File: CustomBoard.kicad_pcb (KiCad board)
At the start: 4 copper layers, 40.9 x 34.1 mm, 24 parts, among them J1 RIGHT, J10 Sensor08, J11 Sensor09, J12 Sensor10, J13 Sensor11, J14 Sensor12, J2 LEFT, J3 Sensor01, J4 Sensor02, J5 Sensor03, J6 Sensor04, J7 Sensor05, J8 Sensor06, J9 Sensor07, U1 DS28E05, U2 PCA9555, U3 VL53L1X

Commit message: routing power lines
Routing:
- net VCC: track 0.00 -> 146.8 mm, vias 0 -> 12
- net GND: track 0.00 -> 138.5 mm, vias 0 -> 12
- net SDA: track 122.2 -> 134.0 mm
- net OW: track 0.00 -> 6.91 mm
- added copper zone on F.Cu, net GND

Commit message: continue routing
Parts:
- added R10: 10k, Resistors_SMD:R_0402, B.Cu at (135.4, 111.7)
- added R11: 10k, Resistors_SMD:R_0402, B.Cu at (127.2, 111.4)
- added R12: 10k, Resistors_SMD:R_0402, B.Cu at (122.6, 103.4)
- added R13: 10k, Resistors_SMD:R_0402, B.Cu at (123.2, 94.2)
- added R14: 10k, Resistors_SMD:R_0402, B.Cu at (125.5, 86.0)
- added R2: 10k, Resistors_SMD:R_0402, B.Cu at (132.9, 82.3)
- added R3: 10k, Resistors_SMD:R_0402, B.Cu at (141.7, 82.3)
- added R5: 10k, Resistors_SMD:R_0402, B.Cu at (150.8, 82.3)
- added R6: 10k, Resistors_SMD:R_0402, B.Cu at (155.6, 90.1)
- added R7: 10k, Resistors_SMD:R_0402, B.Cu at (155.1, 100.4)
- added R8: 10k, Resistors_SMD:R_0402, B.Cu at (152.0, 107.6)
- added R9: 10k, Resistors_SMD:R_0402, B.Cu at (145.5, 111.6)
- J2: footprint Pin_Header_Straight_1x10_Pitch2.00mm_SMD_Pin1Left -> Pin_Headers:Pin_Header_Straight_1x10_Pitch2.00mm_SMD_Pin1Left
- moved J8 38.6 mm to (155.3, 107.3), turned to 45 degrees
- moved J14 38.5 mm to (122.7, 86.7), turned to 225 degrees
- moved J13 31.9 mm to (120.9, 97.0), turned to 270 degrees
- moved J7 31.9 mm to (157.1, 97.0), turned to 90 degrees
- moved J3 31.9 mm to (129.7, 80.6), turned to 180 degrees
- moved J9 31.8 mm to (148.3, 113.3), turned to 0 degrees
- moved J4 17.4 mm to (139.0, 80.6), turned to 180 degrees
- moved J6 17.4 mm to (155.3, 86.7), turned to 135 degrees
- moved J12 17.4 mm to (122.7, 107.3), turned to 315 degrees
- moved J10 17.4 mm to (139.0, 113.3), turned to 0 degrees
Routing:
- net GND: track 138.5 -> 210.2 mm, vias 12 -> 15
- net S03: track 0.00 -> 30.0 mm
- net S04: track 0.00 -> 29.0 mm
- net S05: track 0.00 -> 27.5 mm
- net S06: track 0.00 -> 26.5 mm
- net S07: track 0.00 -> 25.8 mm
- net S02: track 0.00 -> 20.4 mm
- net S01: track 0.00 -> 19.3 mm
- net S08: track 0.00 -> 18.2 mm
- net S09: track 0.00 -> 18.0 mm
- net S12: track 0.00 -> 17.9 mm
- net S10: track 0.00 -> 14.2 mm
- net S11: track 0.00 -> 11.5 mm
- net S15: track 0.00 -> 9.47 mm, vias 0 -> 1
- net VCC: track 146.8 -> 154.1 mm

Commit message: continue routing ..
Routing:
- net VCC: track 154.1 -> 193.6 mm, vias 12 -> 14
- net SCL: track 132.8 -> 160.3 mm, vias 12 -> 14
- net SDA: track 134.0 -> 158.9 mm, vias 12 -> 14
- net Net-(D1-Pad1): track 0.00 -> 23.0 mm, vias 0 -> 2
- net Net-(D1-Pad2): track 0.00 -> 3.44 mm, vias 0 -> 1
- net GND: track 210.2 -> 212.1 mm
- added copper zone on B.Cu, net VCC

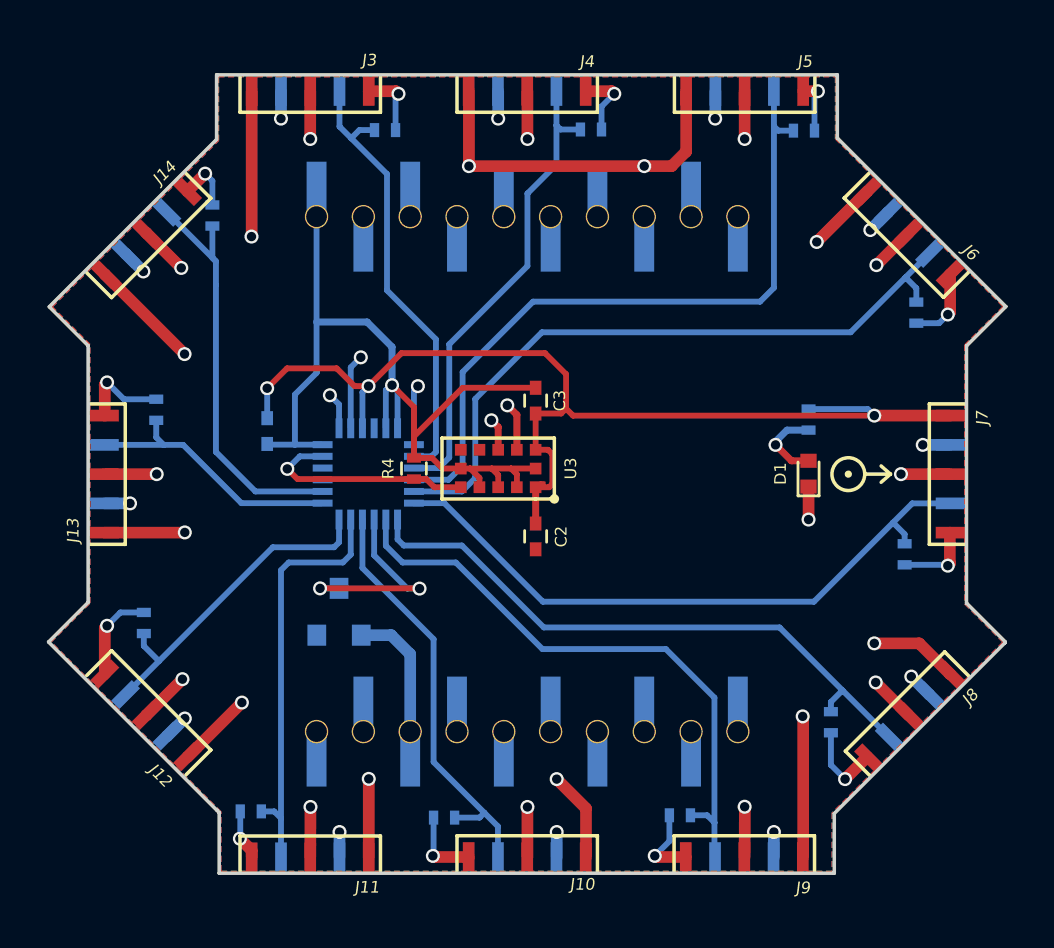
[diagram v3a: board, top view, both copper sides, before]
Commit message: pads missing
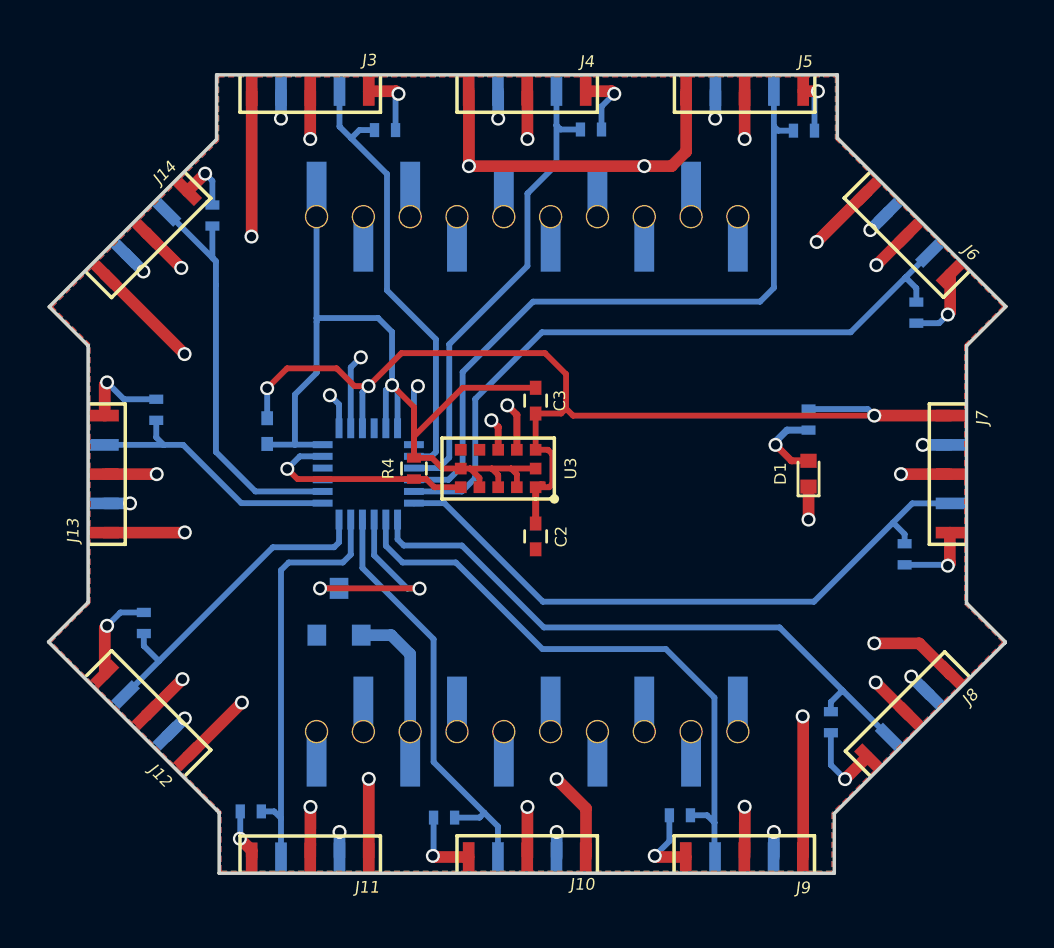
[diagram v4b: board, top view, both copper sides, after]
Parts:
- removed EXP_ORIENTATION: VAL**, crazy2libs:EXP_ORIENTATION
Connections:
- J2 pad 2: (no net) -> Net-(J2-Pad2)
- J2 pad 3: (no net) -> Net-(J2-Pad3)
- J2 pad 6: (no net) -> Net-(J2-Pad6)
- J2 pad 7: (no net) -> Net-(J2-Pad7)
- J2 pad 8: (no net) -> Net-(J2-Pad8)
- J2 pad 9: (no net) -> Net-(J2-Pad9)
- U2 pad 15: S13 -> (no net)
- U2 pad 16: S14 -> (no net)
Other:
- rule trace_min: 0.1 -> 0.05

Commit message: footprints back
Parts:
- J1: footprint Pin_Header_Straight_1x10_Pitch2.00mm_SMD_Pin1Right -> Pin_Headers:Pin_Header_Straight_1x10_Pitch2.00mm_SMD_Pin1Right
- moved C3 0.93 mm to (140.1, 93.3), turned to 180 degrees
- moved C2 0.78 mm to (139.9, 99.1), turned to 0 degrees
- moved J12 0.16 mm to (122.6, 107.4)
- moved J14 0.11 mm to (122.7, 86.6)
- moved J9 0.10 mm to (148.3, 113.5)
- moved J10 0.10 mm to (139.0, 113.5)
- moved J3 0.10 mm to (129.7, 80.5)
- moved J6 0.09 mm to (155.4, 86.6)
- moved J5 0.09 mm to (148.3, 80.5)
- moved J4 0.07 mm to (139.0, 80.6)
- moved J13 0.07 mm to (120.9, 97.0)
- moved J8 0.06 mm to (155.4, 107.4)
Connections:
- J1 pad 1: (no net) -> Net-(J1-Pad1)
- J1 pad 10: (no net) -> Net-(J1-Pad10)
- J1 pad 2: (no net) -> Net-(J1-Pad2)
- J1 pad 3: (no net) -> Net-(J1-Pad3)
- J1 pad 4: (no net) -> Net-(J1-Pad4)
- J1 pad 5: (no net) -> Net-(J1-Pad5)
- J1 pad 6: (no net) -> Net-(J1-Pad6)
- J1 pad 7: (no net) -> Net-(J1-Pad7)
- J1 pad 9: (no net) -> Net-(J1-Pad9)

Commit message: footprints back all
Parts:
- moved C2 0.55 mm to (139.9, 99.7)
- moved C3 0.38 mm to (140.1, 93.7)
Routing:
- net VCC: track 194.0 -> 194.5 mm

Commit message: complete board
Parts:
- J1: footprint Pin_Headers:Pin_Header_Straight_1x10_Pitch2.00mm_SMD_Pin1Right -> footprint:BF090-10-X-B2
- J2: footprint Pin_Headers:Pin_Header_Straight_1x10_Pitch2.00mm_SMD_Pin1Left -> footprint:BF090-10-X-B2
- turned J1 to 180 degrees
- turned J2 to 180 degrees
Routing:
- net SCL: track 160.3 -> 161.9 mm
- net GND: track 212.9 -> 214.5 mm
- net Net-(J2-Pad9): track 0.00 -> 1.60 mm
- net Net-(J2-Pad8): track 0.00 -> 1.60 mm
- net Net-(J2-Pad7): track 0.00 -> 1.60 mm
- net Net-(J2-Pad6): track 0.00 -> 1.60 mm
- net Net-(J2-Pad3): track 0.00 -> 1.60 mm
- net Net-(J2-Pad2): track 0.00 -> 1.60 mm
- net Net-(J1-Pad9): track 0.00 -> 1.60 mm
- net Net-(J1-Pad7): track 0.00 -> 1.60 mm
- net Net-(J1-Pad6): track 0.00 -> 1.60 mm
- net Net-(J1-Pad5): track 0.00 -> 1.60 mm
- net Net-(J1-Pad4): track 0.00 -> 1.60 mm
- net Net-(J1-Pad3): track 0.00 -> 1.60 mm
- net Net-(J1-Pad2): track 0.00 -> 1.60 mm
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
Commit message: camera module
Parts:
- added REF**: AMGCam, footprint:AMGCam, B.Cu at (148.5, 97.0)
- R1: moved to F.Cu
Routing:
- net Net-(D1-Pad1): track 23.0 -> 30.1 mm
- net S04: track 29.5 -> 32.5 mm
- net Net-(D1-Pad2): track 3.44 -> 1.30 mm, vias 1 -> 0
- net S05: track 27.5 -> 29.6 mm
- net VCC: track 196.1 -> 194.5 mm
- net S03: track 30.4 -> 29.6 mm
